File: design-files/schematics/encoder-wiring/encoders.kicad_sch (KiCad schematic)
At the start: 2 parts, among them SW1 RotaryEncoder_Switch, SW2 DualRotaryEncoder_Switch

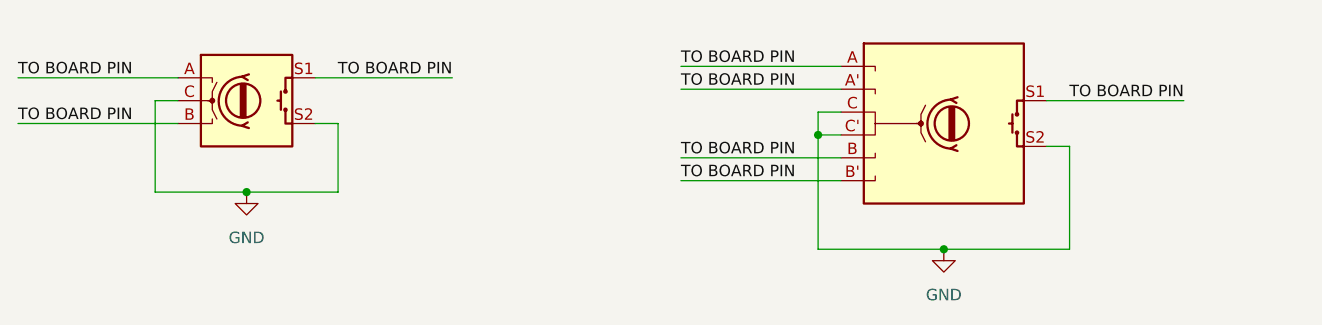
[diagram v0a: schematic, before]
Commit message: Correct wiring diagram (#224)
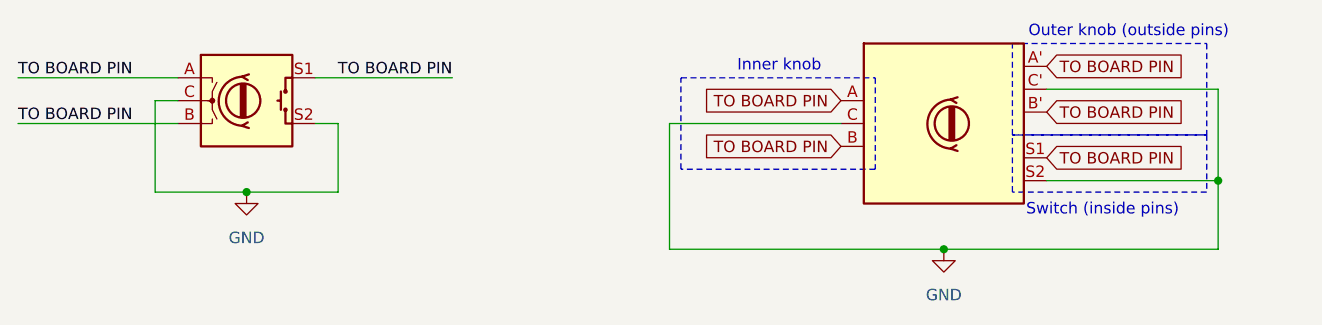
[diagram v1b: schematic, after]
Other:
- note added: "Inner knob"
- note added: "Outer knob (outside pins)"
- note added: "Switch (inside pins)"
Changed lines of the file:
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@@
 	)
 	(junction
-		(at 176.53 99.06)
+		(at 220.98 104.14)
 		(diameter 0)
 		(color 0 0 0 0)
@@
 	(wire
 		(pts
+			(xy 160.02 111.76) (xy 190.5 111.76)
+		)
+		(stroke
+			(width 0)
+			(type default)
+		)
+	)
+	(wire
+		(pts
+			(xy 179.07 97.79) (xy 160.02 97.79)
+		)
+		(stroke
+			(width 0)
+			(type default)
+		)
+	)
+	(wire
+		(pts
 			(xy 120.65 92.71) (xy 135.89 92.71)
 		)
@@
 	(wire
 		(pts
-			(xy 179.07 96.52) (xy 176.53 96.52)
-		)
-		(stroke
-			(width 0)
-			(type default)
-		)
-	)
-	(wire
-		(pts
-			(xy 161.29 93.98) (xy 179.07 93.98)
-		)
-		(stroke
-			(width 0)
-			(type default)
-		)
-	)
-	(wire
-		(pts
-			(xy 176.53 111.76) (xy 190.5 111.76)
-		)
-		(stroke
-			(width 0)
-			(type default)
-		)
-	)
-	(wire
-		(pts
-			(xy 190.5 111.76) (xy 204.47 111.76)
+			(xy 201.93 104.14) (xy 220.98 104.14)
+		)
+		(stroke
+			(width 0)
+			(type default)
+		)
+	)
+	(wire
+		(pts
+			(xy 190.5 111.76) (xy 220.98 111.76)
 		)
 		(stroke
@@
 	(wire
 		(pts
-			(xy 176.53 96.52) (xy 176.53 99.06)
-		)
-		(stroke
-			(width 0)
-			(type default)
-		)
-	)
-	(wire
-		(pts
 			(xy 120.65 97.79) (xy 123.19 97.79)
 		)
@@
 	(wire
 		(pts
+			(xy 220.98 104.14) (xy 220.98 111.76)
+		)
+		(stroke
+			(width 0)
+			(type default)
+		)
+	)
+	(wire
+		(pts
 			(xy 102.87 105.41) (xy 113.03 105.41)
 		)
@@
 	(wire
 		(pts
-			(xy 201.93 95.25) (xy 217.17 95.25)
-		)
-		(stroke
-			(width 0)
-			(type default)
-		)
-	)
-	(wire
-		(pts
 			(xy 87.63 97.79) (xy 105.41 97.79)
 		)
@@
 	(wire
 		(pts
-			(xy 161.29 104.14) (xy 179.07 104.14)
-		)
-		(stroke
-			(width 0)
-			(type default)
-		)
-	)
-	(wire
-		(pts
-			(xy 204.47 100.33) (xy 204.47 111.76)
-		)
-		(stroke
-			(width 0)
-			(type default)
-		)
-	)
-	(wire
-		(pts
 			(xy 102.87 95.25) (xy 102.87 105.41)
 		)
@@
 	(wire
 		(pts
-			(xy 201.93 100.33) (xy 204.47 100.33)
-		)
-		(stroke
-			(width 0)
-			(type default)
-		)
-	)
-	(wire
-		(pts
-			(xy 161.29 91.44) (xy 179.07 91.44)
-		)
-		(stroke
-			(width 0)
-			(type default)
-		)
-	)
-	(wire
-		(pts
-			(xy 161.29 101.6) (xy 179.07 101.6)
-		)
-		(stroke
-			(width 0)
-			(type default)
-		)
-	)
-	(wire
-		(pts
-			(xy 176.53 99.06) (xy 176.53 111.76)
-		)
-		(stroke
-			(width 0)
-			(type default)
-		)
-	)
-	(wire
-		(pts
-			(xy 179.07 99.06) (xy 176.53 99.06)
-		)
-		(stroke
-			(width 0)
-			(type default)
+			(xy 201.93 93.98) (xy 220.98 93.98)
+		)
+		(stroke
+			(width 0)
+			(type default)
+		)
+	)
+	(wire
+		(pts
+			(xy 220.98 93.98) (xy 220.98 104.14)
+		)
+		(stroke
+			(width 0)
+			(type default)
+		)
+	)
+	(wire
+		(pts
+			(xy 160.02 97.79) (xy 160.02 111.76)
+		)
+		(stroke
+			(width 0)
+			(type default)
+		)
+	)
+	(rectangle
+		(start 161.29 92.71)
+		(end 182.88 102.87)
+		(stroke
+			(width 0)
+			(type dot)
+		)
+		(fill
+			(type none)
+		)
+	)
+	(rectangle
+		(start 198.12 99.06)
+		(end 219.71 105.41)
+		(stroke
+			(width 0)
+			(type dot)
+		)
+		(fill
+			(type none)
+		)
+	)
+	(rectangle
+		(start 198.12 88.9)
+		(end 219.71 99.06)
+		(stroke
+			(width 0)
+			(type dot)
+		)
+		(fill
+			(type none)
+		)
+	)
+	(text "Inner knob"
+		(exclude_from_sim no)
+		(at 172.212 91.44 0)
+		(effects
+			(font
+				(size 1.27 1.27)
+			)
+		)
+	)
+	(text "Switch (inside pins)"
+		(exclude_from_sim no)
+		(at 199.644 107.442 0)
+		(effects
+			(font
+				(size 1.27 1.27)
+			)
+			(justify left)
+		)
+	)
+	(text "Outer knob (outside pins)"
+		(exclude_from_sim no)
+		(at 199.898 87.63 0)
+		(effects
+			(font
+				(size 1.27 1.27)
+			)
+			(justify left)
 		)
 	)
@@
 		)
 	)
-	(label "TO BOARD PIN"
-		(at 161.29 91.44 0)
-		(effects
-			(font
-				(size 1.27 1.27)
-			)
-			(justify left bottom)
-		)
-	)
-	(label "TO BOARD PIN"
-		(at 217.17 95.25 180)
-		(effects
-			(font
-				(size 1.27 1.27)
-			)
-			(justify right bottom)
-		)
-	)
-	(label "TO BOARD PIN"
-		(at 161.29 93.98 0)
-		(effects
-			(font
-				(size 1.27 1.27)
-			)
-			(justify left bottom)
-		)
-	)
-	(label "TO BOARD PIN"
-		(at 161.29 101.6 0)
-		(effects
-			(font
-				(size 1.27 1.27)
-			)
-			(justify left bottom)
-		)
-	)
-	(label "TO BOARD PIN"
-		(at 161.29 104.14 0)
-		(effects
-			(font
-				(size 1.27 1.27)
-			)
-			(justify left bottom)
-		)
-	)
+	(global_label "TO BOARD PIN"
+		(shape input)
+		(at 179.07 100.33 180)
+		(fields_autoplaced yes)
+		(effects
+			(font
+				(size 1.27 1.27)
+			)
+			(justify right)
+		)
+		(property "Intersheetrefs" "${INTERSHEET_REFS}"
+			(at 162.4171 100.33 0)
+			(effects
+				(font
+					(size 1.27 1.27)
+				)
+				(justify right)
+				(hide yes)
+			)
+		)
+	)
+	(global_label "TO BOARD PIN"
+		(shape input)
+		(at 201.93 101.6 0)
+		(fields_autoplaced yes)
+		(effects
+			(font
+				(size 1.27 1.27)
+			)
+			(justify left)
+		)
+		(property "Intersheetrefs" "${INTERSHEET_REFS}"
+			(at 218.5829 101.6 0)
+			(effects
+				(font
+					(size 1.27 1.27)
+				)
+				(justify left)
+				(hide yes)
+			)
+		)
+	)
+	(global_label "TO BOARD PIN"
+		(shape input)
+		(at 201.93 91.44 0)
+		(fields_autoplaced yes)
+		(effects
+			(font
+				(size 1.27 1.27)
+			)
+			(justify left)
+		)
+		(property "Intersheetrefs" "${INTERSHEET_REFS}"
+			(at 218.5829 91.44 0)
+			(effects
+				(font
+					(size 1.27 1.27)
+				)
+				(justify left)
+				(hide yes)
+			)
+		)
+	)
+	(global_label "TO BOARD PIN"
+		(shape input)
+		(at 201.93 96.52 0)
+		(fields_autoplaced yes)
+		(effects
+			(font
+				(size 1.27 1.27)
+			)
+			(justify left)
+		)
+		(property "Intersheetrefs" "${INTERSHEET_REFS}"
+			(at 218.5829 96.52 0)
+			(effects
+				(font
+					(size 1.27 1.27)
+				)
+				(justify left)
+				(hide yes)
+			)
+		)
+	)
+	(global_label "TO BOARD PIN"
+		(shape input)
+		(at 179.07 95.25 180)
+		(fields_autoplaced yes)
+		(effects
+			(font
+				(size 1.27 1.27)
+			)
+			(justify right)
+		)
+		(property "Intersheetrefs" "${INTERSHEET_REFS}"
+			(at 162.4171 95.25 0)
+			(effects
+				(font
+					(size 1.27 1.27)
+				)
+				(justify right)
+				(hide yes)
+			)
+		)
+	)
